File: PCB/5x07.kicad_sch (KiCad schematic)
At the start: 21 parts, among them J1 AVR-ISP-6, SW1 SW_Push, U1 ATmega32U4-A, U2 PRTR5V0U2X, Y1 16MHz

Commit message: v2: reversiblility for LHS and RHS
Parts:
- SW1: footprint Button_Switch_SMD:SW_SPST_SKQG_WithStem -> assets:SW_SPST_SKQG_WithStem_Reversible
- USB1: footprint Type-C:HRO-TYPE-C-31-M-12-HandSoldering -> assets:HRO-TYPE-C-31-M-12-HandSoldering-Reversible

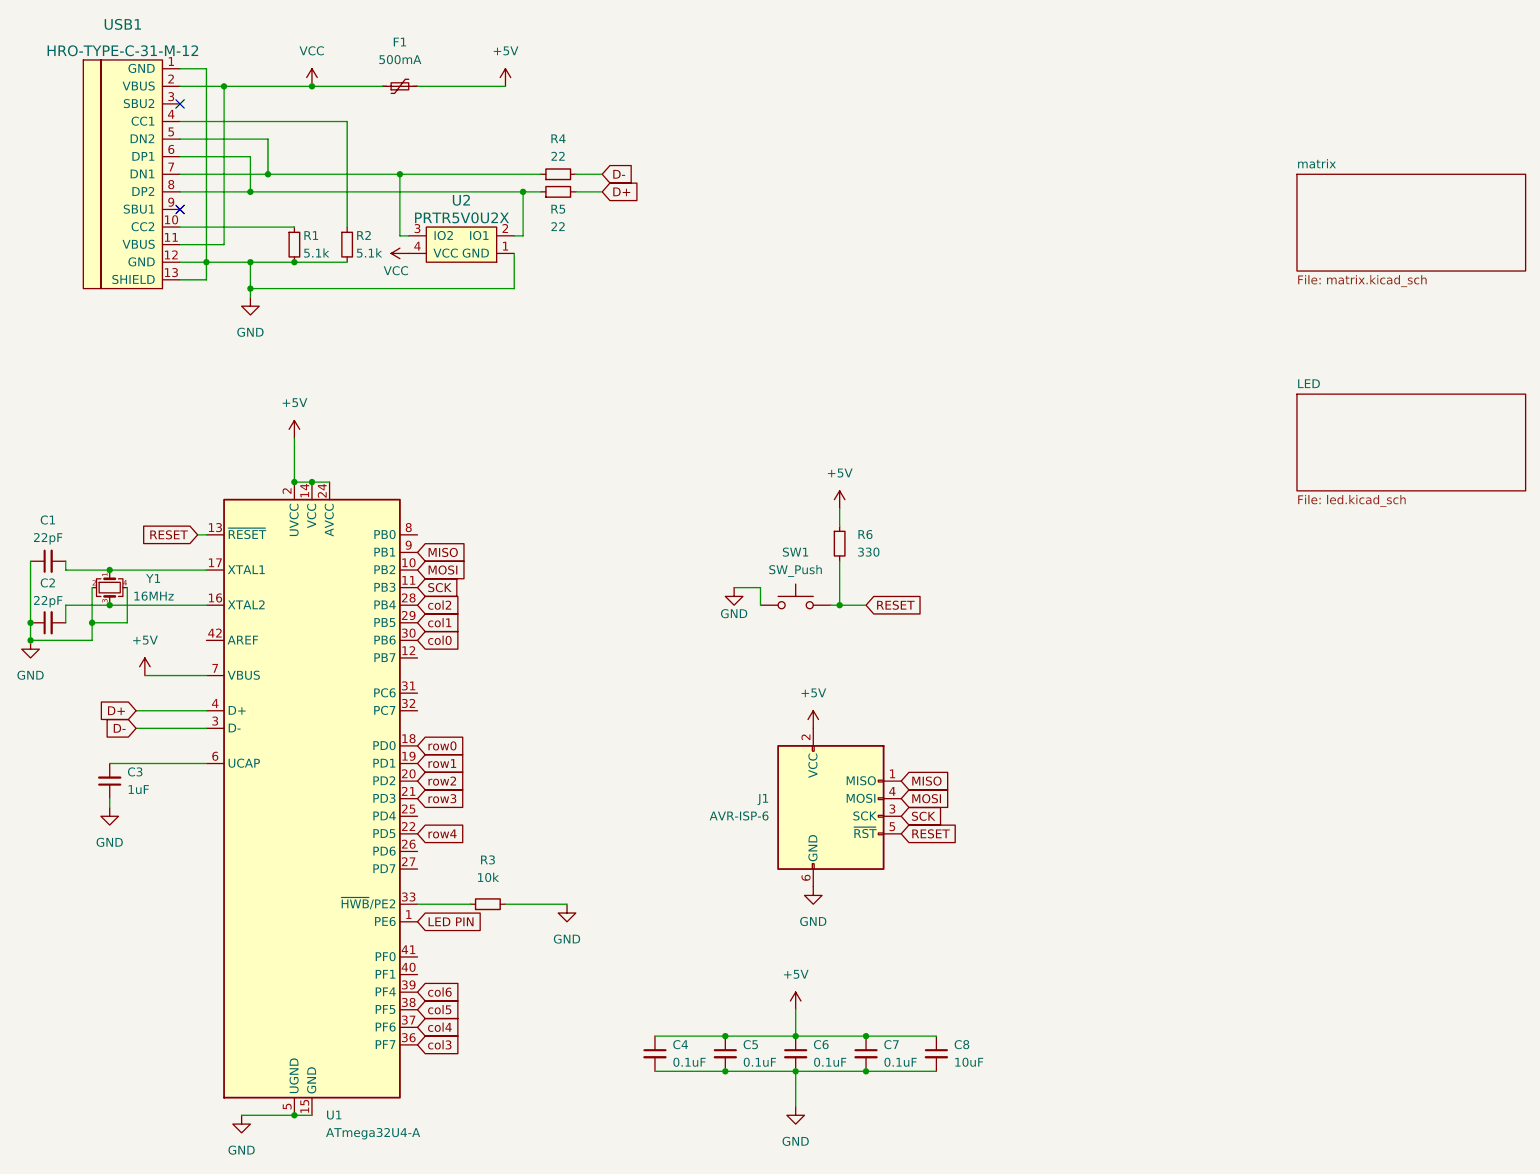
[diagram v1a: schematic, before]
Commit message: v3: TRRS for split sides
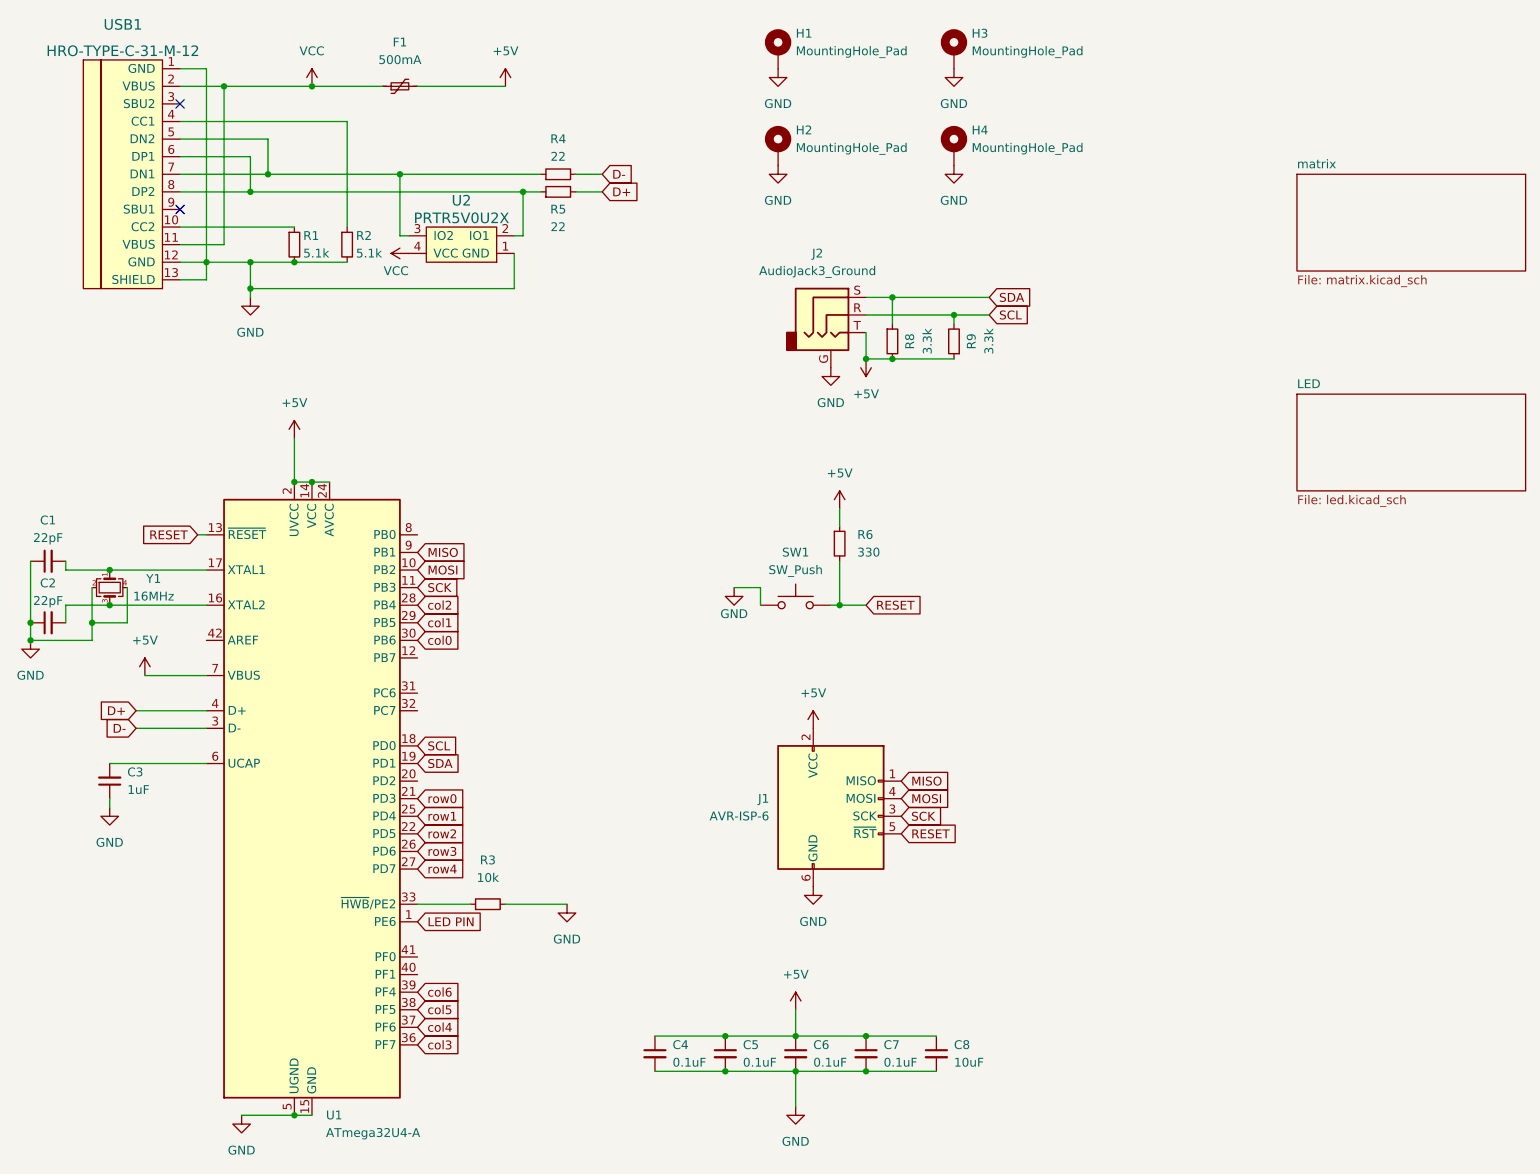
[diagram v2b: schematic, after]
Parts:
- added H1, H2, H3, H4: MountingHole_Pad, random-keyboard-parts:Generic-Mounthole, symbol Mechanical:MountingHole_Pad
- added J2: AudioJack3_Ground, assets:PJ-3200B-4A-Reversible, symbol Connector:AudioJack3_Ground
- added R8, R9: 3.3k, Resistor_SMD:R_0805_2012Metric_Pad1.20x1.40mm_HandSolder, symbol Device:R_Small
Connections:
- net +5V: now also J2.T, R8.2, R9.1
- net GND: now also H1.1, H2.1, H3.1, H4.1, J2.G
- net row0: now also U1.21 (PD3); no longer U1.18 (PD0)
- net row1: now also U1.25 (PD4); no longer U1.19 (PD1)
- net row2: now also U1.22 (PD5); no longer U1.20 (PD2)
- net row3: now also U1.26 (PD6); no longer U1.21 (PD3)
- net row4: now also U1.27 (PD7); no longer U1.22 (PD5)
- new net SCL: J2.R, R9.2, U1.18 (PD0)
- new net SDA: J2.S, R8.1, U1.19 (PD1)

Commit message: bugfix
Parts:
- J1: footprint random-keyboard-parts:Reset_Pretty-Mask -> random-keyboard-parts:Reset_Pretty
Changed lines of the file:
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@@
       (effects (font (size 1.27 1.27)) (justify right))
     )
-    (property "Footprint" "random-keyboard-parts:Reset_Pretty-Mask" (id 2) (at 134.62 142.24 90)
+    (property "Footprint" "random-keyboard-parts:Reset_Pretty" (id 2) (at 134.62 142.24 90)
       (effects (font (size 1.27 1.27)) hide)
     )
@@
     )
     (path "/e5bff2ed-4470-4084-a621-480b9de3ee53"
-      (reference "J1") (unit 1) (value "AVR-ISP-6") (footprint "random-keyboard-parts:Reset_Pretty-Mask")
+      (reference "J1") (unit 1) (value "AVR-ISP-6") (footprint "random-keyboard-parts:Reset_Pretty")
     )
     (path "/332de923-a953-48c5-8038-c90a3d96a3d1"

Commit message: minified TRRS jack footprint and other bugfixes
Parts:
- J2: footprint assets:PJ-3200B-4A-Reversible -> assets:PJ-3200B-4A-Reversible-Mini
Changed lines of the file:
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@@
     (property "Reference" "J2" (id 0) (at 139.065 62.23 0))
     (property "Value" "AudioJack3_Ground" (id 1) (at 139.065 64.77 0))
-    (property "Footprint" "assets:PJ-3200B-4A-Reversible" (id 2) (at 140.97 71.12 0)
+    (property "Footprint" "assets:PJ-3200B-4A-Reversible-Mini" (id 2) (at 140.97 71.12 0)
       (effects (font (size 1.27 1.27)) hide)
     )
@@
     )
     (path "/332de923-a953-48c5-8038-c90a3d96a3d1"
-      (reference "J2") (unit 1) (value "AudioJack3_Ground") (footprint "assets:PJ-3200B-4A-Reversible")
+      (reference "J2") (unit 1) (value "AudioJack3_Ground") (footprint "assets:PJ-3200B-4A-Reversible-Mini")
     )
     (path "/4787577f-7d8a-45a2-be7c-203d64397828/b8baca79-5620-4f40-beee-40a42b9669e9"

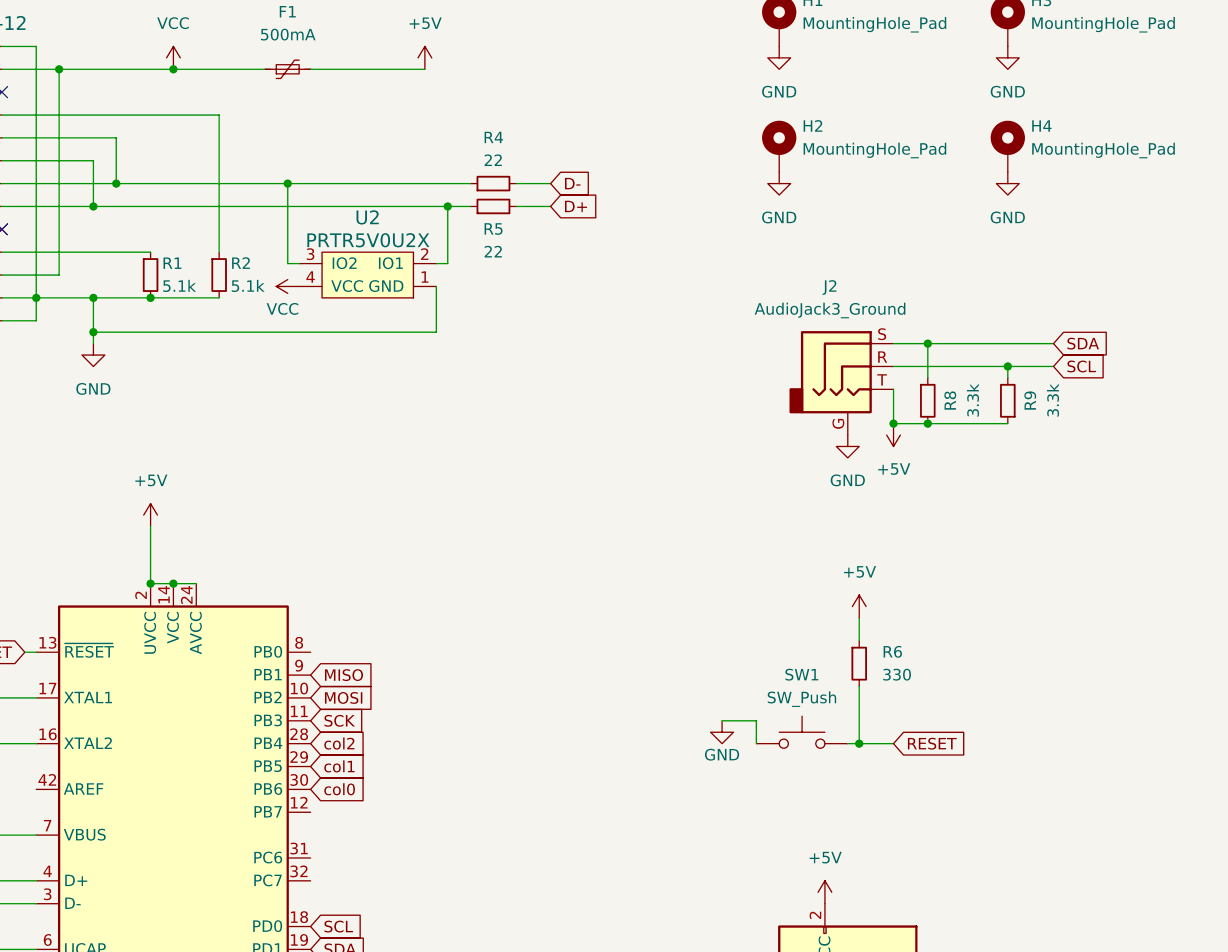
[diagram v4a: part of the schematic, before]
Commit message: added build pics and instructions
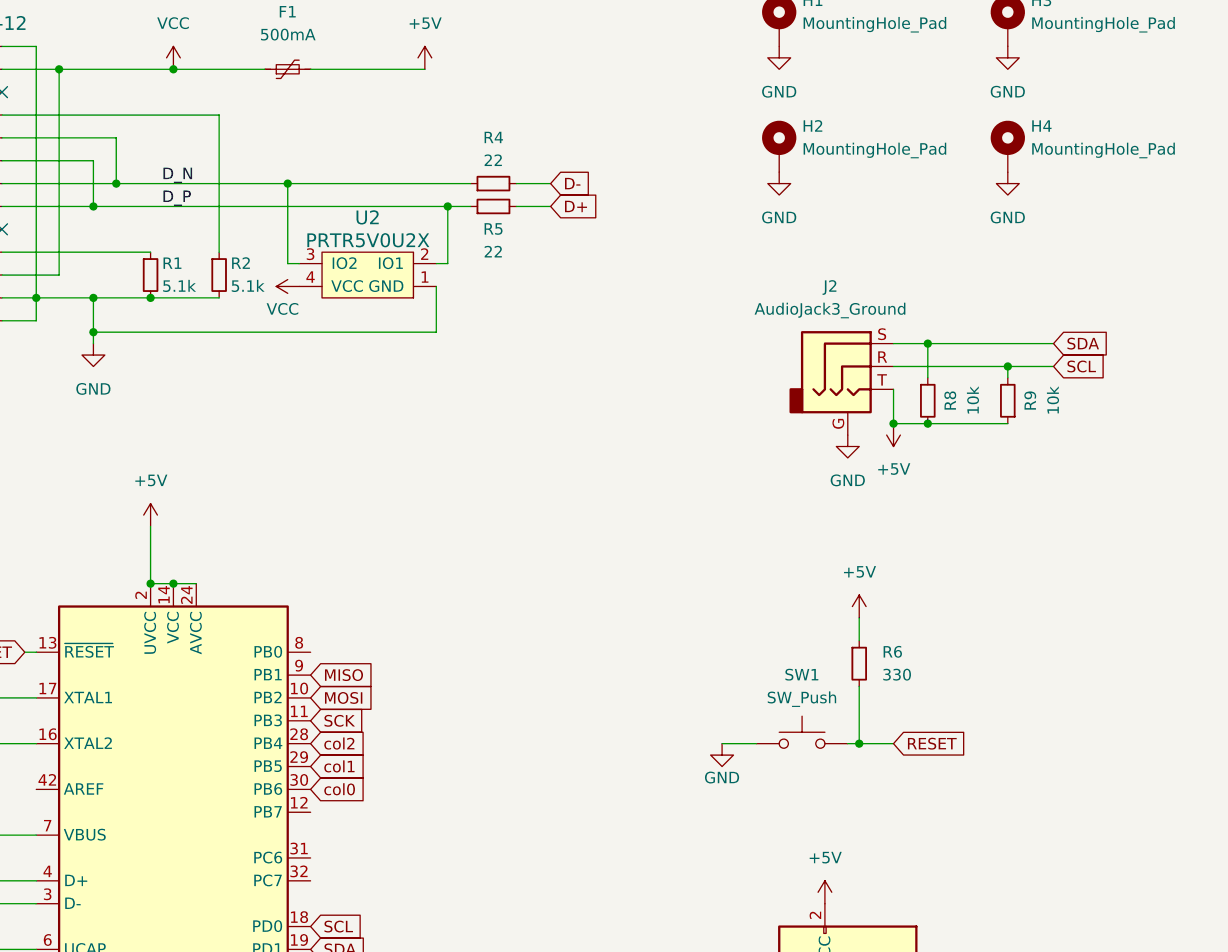
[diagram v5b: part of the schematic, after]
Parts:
- R8, R9: value 3.3k -> 10k
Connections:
- net D_N: now reaches R4.1, U2.3 (IO2), USB1.5 (DN2), USB1.7 (DN1)
- net D_P: now reaches R5.1, U2.2 (IO1), USB1.6 (DP1), USB1.8 (DP2)
